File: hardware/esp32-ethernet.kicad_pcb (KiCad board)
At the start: 4 copper layers, 80 x 40 mm, 132 parts, among them J101 USB-C-2, P101 EXT_HEADER, P201 CON-SENSOR2, P202 CON-SENSOR2, P203 CON-SENSOR2, P204 CON-SENSOR2, P205 CON-SENSOR2, P206 CON-SENSOR2, P301 POE, P302 RJPSL-001TA1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

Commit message: version 1.2
 change poe header to standard
 change Ethernet mounting vias position
 change 1uF capacitors to 0603
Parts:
- C101, C102: footprint kicad-libraries:C0402F -> kicad-libraries:C0603F
- P301: footprint kicad-libraries:pin_array_5x1 -> kicad-libraries:pin_array_1x5-P2mm_D1mm
- moved C101 0.36 mm to (151.0, 154.1)
- moved C102 0.10 mm to (155.1, 154.3)
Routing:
- net SHD: track 20.8 -> 29.9 mm, vias 12 -> 10
- net Net-(C101-Pad2): track 22.5 -> 21.1 mm
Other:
- board text added: "ESP32 Ethernet 1.2"
- board text removed: "ESP32 Ethernet 1.1"

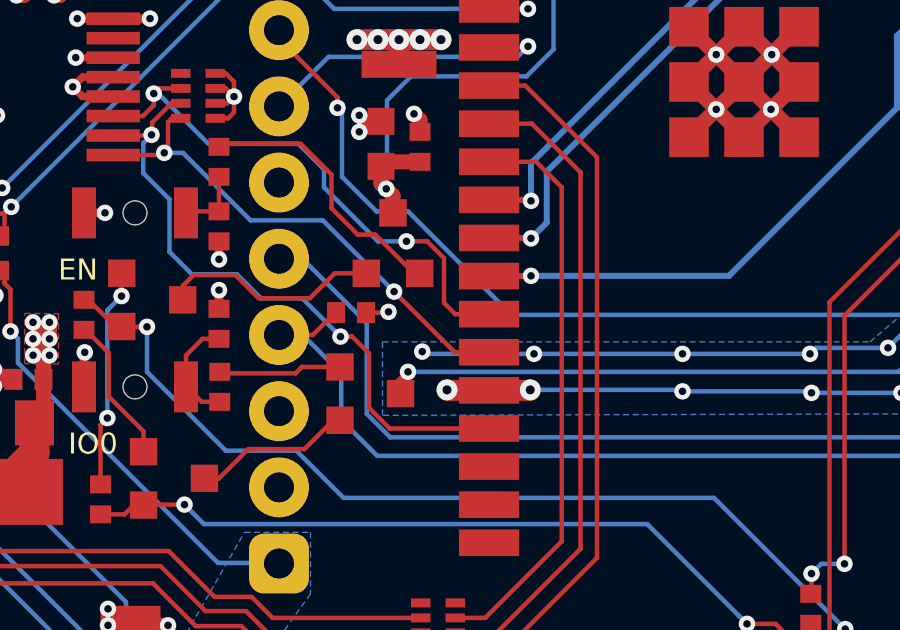
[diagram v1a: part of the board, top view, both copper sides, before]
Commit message: bugfix: add missing 20k GPIO0 strapping resistor
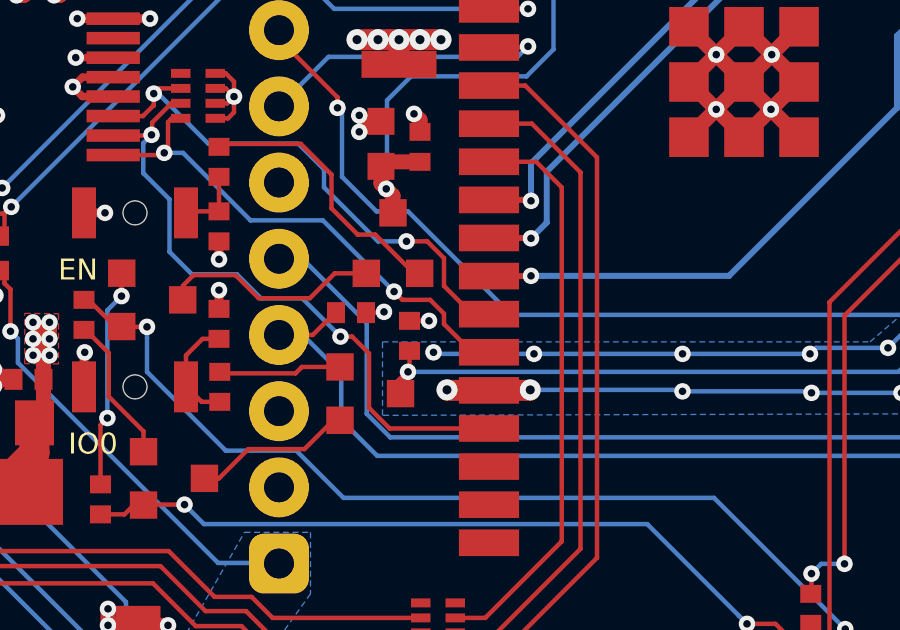
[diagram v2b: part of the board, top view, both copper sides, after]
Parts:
- added R102: 20k, kicad-libraries:R0402F, F.Cu at (155.7, 141.3)
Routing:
- net ESP_IO0: track 41.9 -> 42.7 mm
- net 3V3: track 68.9 -> 69.6 mm, vias 49 -> 50
- net GND: track 261.9 -> 261.4 mm

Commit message: version 1.2 - change ethernet jack
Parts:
- removed P301: POE, kicad-libraries:pin_array_1x5-P2mm_D1mm
- removed P302: RJPSL-001TA1, kicad-libraries:RJPSL-001TA1
- added J301: RJSL-009TA1, kicad-libraries:RJSL-009TA1, F.Cu at (186.5, 148.2)
- moved R315 13.8 mm to (178.2, 139.1)
- moved R316 1.00 mm to (175.5, 152.8)
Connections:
- R315 pad 1: LED_GREEN -> GND
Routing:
- net Net-(P301-Pad3): track 31.8 -> 0.00 mm, vias 2 -> 0
- net Net-(P301-Pad4): track 29.3 -> 0.00 mm, vias 2 -> 0
- net Net-(P301-Pad1): track 22.8 -> 0.00 mm, vias 2 -> 0
- net Net-(P301-Pad2): track 16.2 -> 0.00 mm, vias 2 -> 0
- net LED_GREEN: track 41.7 -> 35.5 mm
- net SHD: track 29.9 -> 26.3 mm
- net Net-(C313-Pad2): track 5.51 -> 3.25 mm
- net RXIP: track 7.71 -> 9.60 mm
- net Net-(J301-Pad3): track 14.5 -> 16.0 mm
- net yellowLED: track 26.9 -> 25.9 mm
- net GND: track 261.4 -> 262.3 mm, vias 191 -> 192
- net Net-(J301-Pad2): track 9.06 -> 9.89 mm
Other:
- board text removed: "P1"
- board text removed: "P2"
- board text removed: "P3"
- board text removed: "P4"
- board text removed: "PoE"
- board text removed: "SHD"
